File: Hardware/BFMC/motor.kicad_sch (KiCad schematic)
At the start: 28 parts, among them J4 MOTOR_BLDC, J5 MOTOR_STEERING, J6 MOTOR_CAMERA, Q1 BSN20, Q2 BSN20, Q3 BSN20

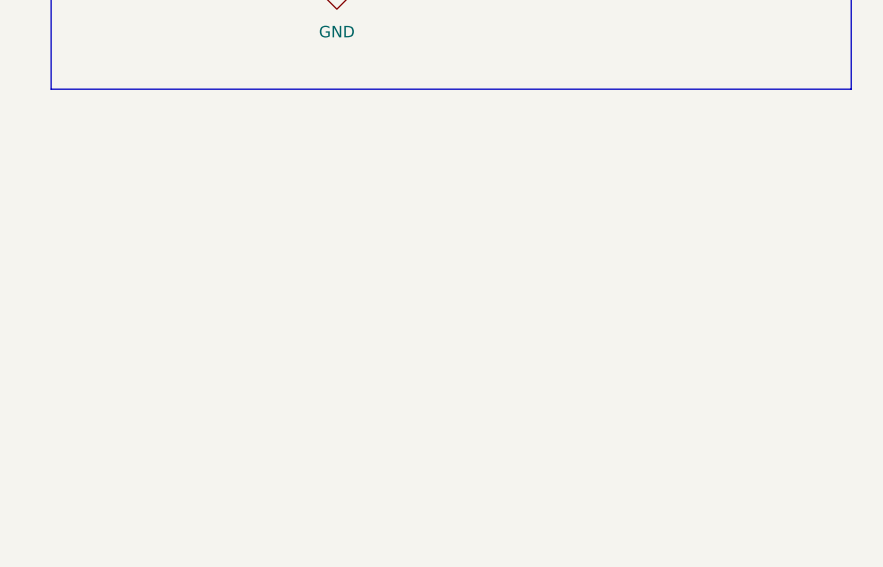
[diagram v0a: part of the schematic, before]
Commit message: update temporary file in stm32
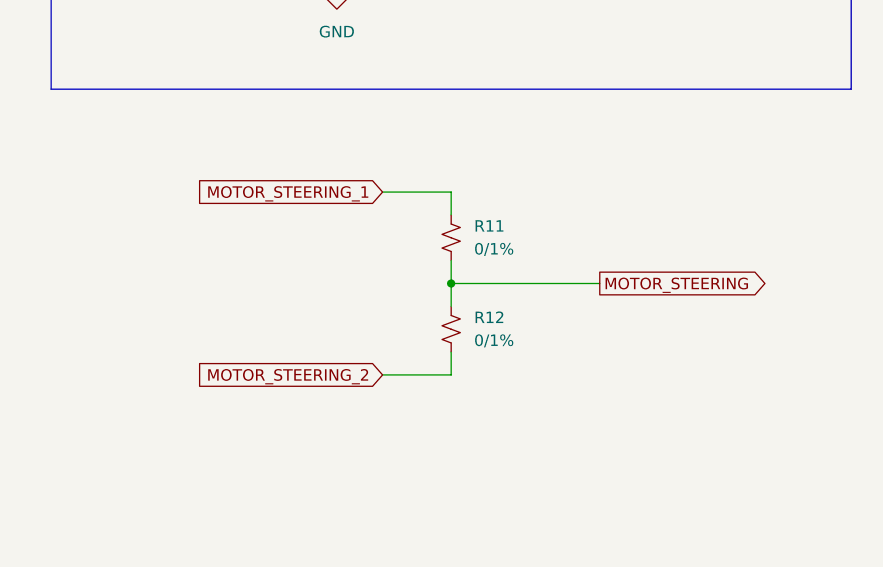
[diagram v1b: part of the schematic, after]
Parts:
- added R11, R12: 0/1%, Resistor_SMD:R_0603_1608Metric_Pad0.98x0.95mm_HandSolder, symbol Device:R_Small_US
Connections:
- net MOTOR_STEERING: now also R11.2, R12.1
- new net MOTOR_STEERING_1: R11.1
- new net MOTOR_STEERING_2: R12.2
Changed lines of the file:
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@@
   (junction (at 49.53 175.26) (diameter 0) (color 0 0 0 0)
   )
+  (junction (at 209.55 135.89) (diameter 0) (color 0 0 0 0)
+  )
   (junction (at 196.85 54.61) (diameter 0) (color 0 0 0 0)
   )
@@
     (stroke (width 0) (type default))
   )
+  (wire (pts (xy 201.93 125.73) (xy 209.55 125.73))
+    (stroke (width 0) (type default))
+  )
   (wire (pts (xy 49.53 139.7) (xy 64.77 139.7))
     (stroke (width 0) (type default))
@@
     (stroke (width 0) (type default))
   )
+  (wire (pts (xy 209.55 135.89) (xy 209.55 138.43))
+    (stroke (width 0) (type default))
+  )
   (wire (pts (xy 91.44 68.58) (xy 91.44 73.66))
     (stroke (width 0) (type default))
   )
+  (wire (pts (xy 209.55 133.35) (xy 209.55 135.89))
+    (stroke (width 0) (type default))
+  )
   (wire (pts (xy 64.77 80.01) (xy 64.77 77.47))
     (stroke (width 0) (type default))
@@
     (stroke (width 0) (type default))
   )
+  (wire (pts (xy 201.93 146.05) (xy 209.55 146.05))
+    (stroke (width 0) (type default))
+  )
   (wire (pts (xy 64.77 36.83) (xy 80.01 36.83))
     (stroke (width 0) (type default))
@@
     (stroke (width 0) (type default))
   )
+  (wire (pts (xy 209.55 125.73) (xy 209.55 128.27))
+    (stroke (width 0) (type default))
+  )
   (wire (pts (xy 33.02 146.05) (xy 33.02 147.32))
     (stroke (width 0) (type default))
@@
     (stroke (width 0) (type default))
   )
+  (wire (pts (xy 209.55 146.05) (xy 209.55 143.51))
+    (stroke (width 0) (type default))
+  )
   (wire (pts (xy 55.88 80.01) (xy 64.77 80.01))
     (stroke (width 0) (type default))
@@
   )
   (wire (pts (xy 74.93 46.99) (xy 64.77 46.99))
+    (stroke (width 0) (type default))
+  )
+  (wire (pts (xy 226.06 135.89) (xy 209.55 135.89))
     (stroke (width 0) (type default))
   )
@@
     )
   )
+  (global_label "MOTOR_STEERING" (shape output) (at 226.06 135.89 0) (fields_autoplaced)
+    (effects (font (size 1.27 1.27)) (justify left))
+    (property "Intersheetrefs" "${INTERSHEET_REFS}" (at 245.3132 135.89 0)
+      (effects (font (size 1.27 1.27)) (justify left) hide)
+    )
+  )
+  (global_label "MOTOR_STEERING_1" (shape input) (at 201.93 125.73 180) (fields_autoplaced)
+    (effects (font (size 1.27 1.27)) (justify right))
+    (property "Intersheetrefs" "${INTERSHEET_REFS}" (at 180.4997 125.73 0)
+      (effects (font (size 1.27 1.27)) (justify right) hide)
+    )
+  )
   (global_label "MOTOR_CAMERA_CO" (shape output) (at 102.87 109.22 0) (fields_autoplaced)
     (effects (font (size 1.27 1.27)) (justify left))
@@
     )
   )
+  (global_label "MOTOR_STEERING_2" (shape input) (at 201.93 146.05 180) (fields_autoplaced)
+    (effects (font (size 1.27 1.27)) (justify right))
+    (property "Intersheetrefs" "${INTERSHEET_REFS}" (at 180.4997 146.05 0)
+      (effects (font (size 1.27 1.27)) (justify right) hide)
+    )
+  )
   (global_label "MOTOR_STEERING_CO" (shape output) (at 102.87 80.01 0) (fields_autoplaced)
     (effects (font (size 1.27 1.27)) (justify left))
@@
     )
   )
+  (symbol (lib_id "Device:R_Small_US") (at 209.55 130.81 0) (unit 1)
+    (in_bom yes) (on_board yes) (dnp no) (fields_autoplaced)
+    (property "Reference" "R11" (at 212.09 129.54 0)
+      (effects (font (size 1.27 1.27)) (justify left))
+    )
+    (property "Value" "0/1%" (at 212.09 132.08 0)
+      (effects (font (size 1.27 1.27)) (justify left))
+    )
+    (property "Footprint" "Resistor_SMD:R_0603_1608Metric_Pad0.98x0.95mm_HandSolder" (at 209.55 130.81 0)
+      (effects (font (size 1.27 1.27)) hide)
+    )
+    (property "Datasheet" "~" (at 209.55 130.81 0)
+      (effects (font (size 1.27 1.27)) hide)
+    )
+    (property "URL" "https://www.thegioiic.com/dien-tro-0-ohm-0603-1-" (at 209.55 130.81 0)
+      (effects (font (size 1.27 1.27)) hide)
+    )
+    (pin "1")
+    (pin "2")
+    (instances
+      (project "BFMC"
+        (path "/a702f17a-d8b6-4710-aaf3-998facd86d1b/c4165175-c24d-4996-a606-be543c2429f2"
+          (reference "R11") (unit 1)
+        )
+      )
+    )
+  )
   (symbol (lib_id "Device:R_Small_US") (at 91.44 105.41 0) (unit 1)
     (in_bom yes) (on_board yes) (dnp no) (fields_autoplaced)
@@
         )
       )
+    )
+  )
+  (symbol (lib_id "Device:R_Small_US") (at 209.55 140.97 0) (unit 1)
+    (in_bom yes) (on_board yes) (dnp no) (fields_autoplaced)
+    (property "Reference" "R12" (at 212.09 139.7 0)
+      (effects (font (size 1.27 1.27)) (justify left))
+    )
+    (property "Value" "0/1%" (at 212.09 142.24 0)
+      (effects (font (size 1.27 1.27)) (justify left))
+    )
+    (property "Footprint" "Resistor_SMD:R_0603_1608Metric_Pad0.98x0.95mm_HandSolder" (at 209.55 140.97 0)
+      (effects (font (size 1.27 1.27)) hide)
+    )
+    (property "Datasheet" "~" (at 209.55 140.97 0)
+      (effects (font (size 1.27 1.27)) hide)
+    )
+    (property "URL" "https://www.thegioiic.com/dien-tro-0-ohm-0603-1-" (at 209.55 140.97 0)
+      (effects (font (size 1.27 1.27)) hide)
+    )
+    (pin "1")
+    (pin "2")
+    (instances
+      (project "BFMC"
+        (path "/a702f17a-d8b6-4710-aaf3-998facd86d1b/c4165175-c24d-4996-a606-be543c2429f2"
+          (reference "R12") (unit 1)
+        )
+      )
